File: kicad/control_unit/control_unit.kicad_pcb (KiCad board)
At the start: 2 copper layers, 23 parts

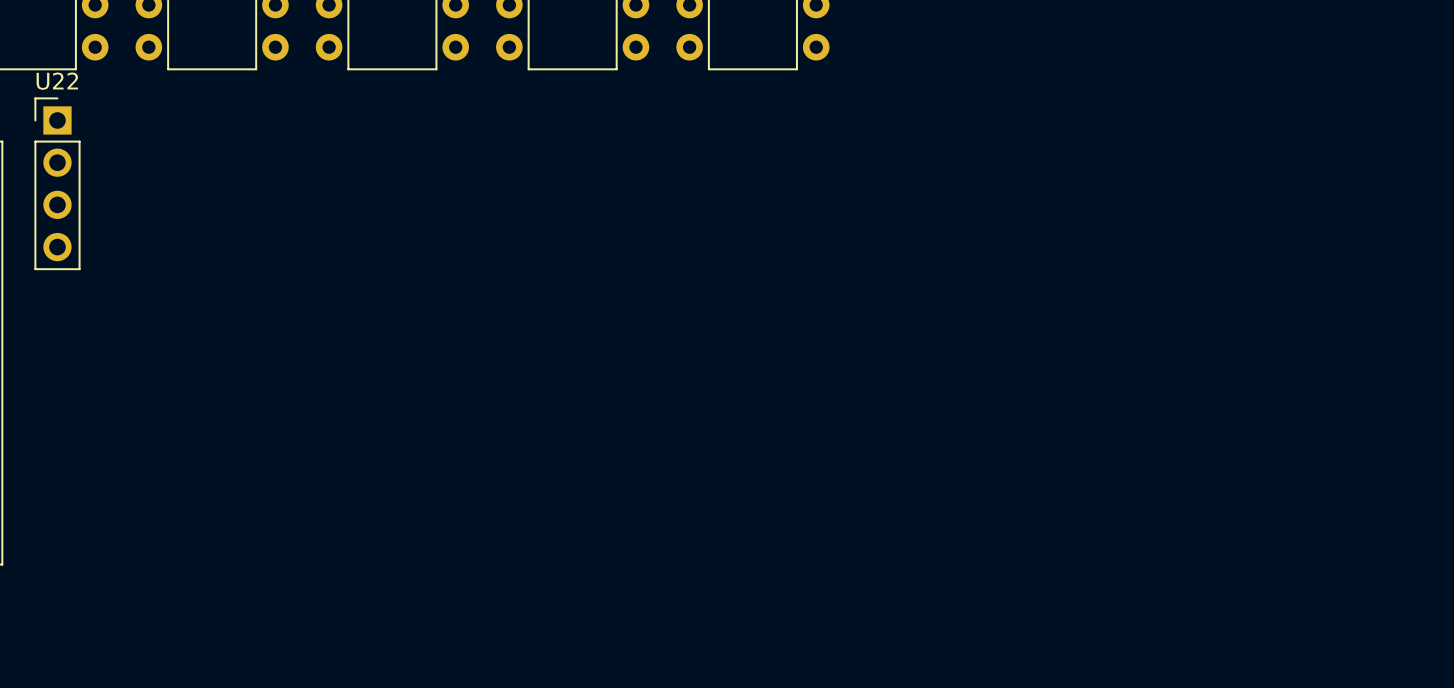
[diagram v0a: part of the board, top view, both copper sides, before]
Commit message: Added pullup resistors to control unit memory address
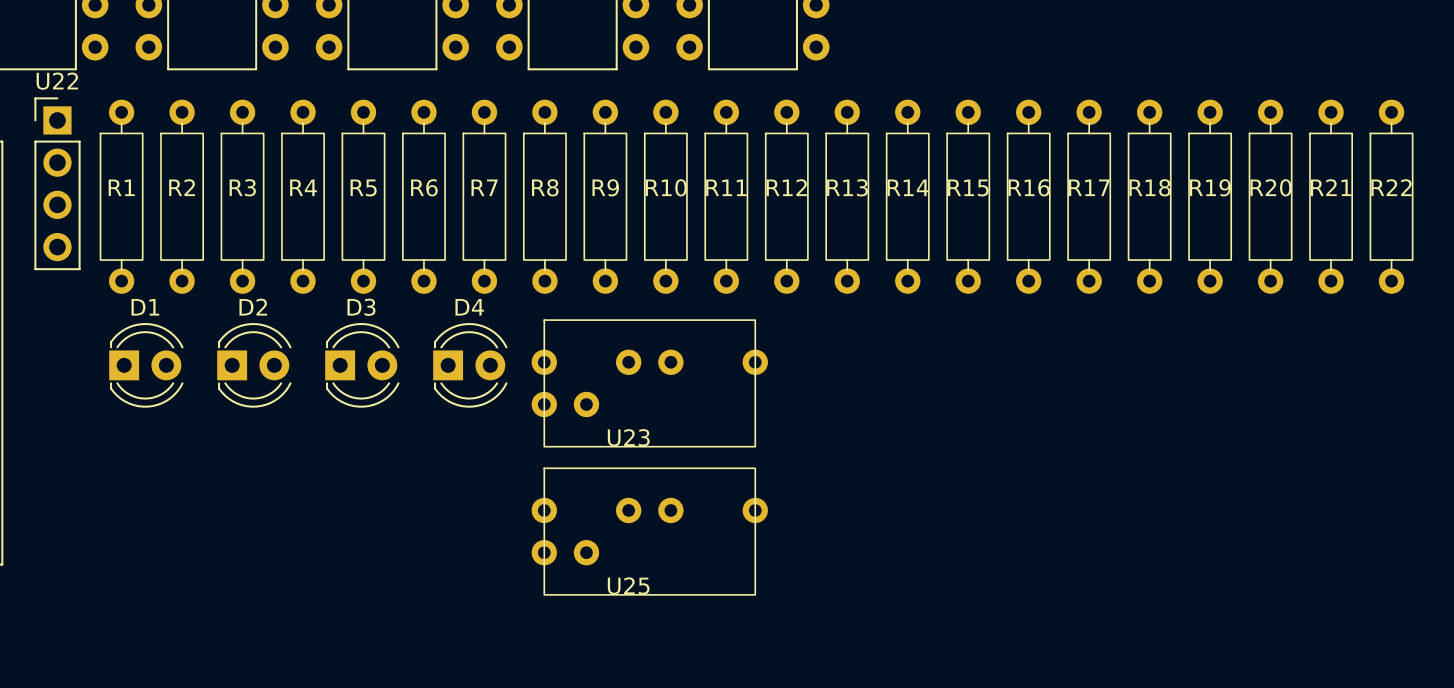
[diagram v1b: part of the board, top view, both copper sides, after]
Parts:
- added D1: LED, LED_THT:LED_D4.0mm, F.Cu at (138.3, 137.2)
- added D2: LED, LED_THT:LED_D4.0mm, F.Cu at (144.8, 137.2)
- added D3: LED, LED_THT:LED_D4.0mm, F.Cu at (151.3, 137.2)
- added D4: LED, LED_THT:LED_D4.0mm, F.Cu at (157.8, 137.2)
- added R1: 10k, custom_footprint_library:0.4_pitch_resistor, F.Cu at (138.2, 127.0)
- added R10: 10k, custom_footprint_library:0.4_pitch_resistor, F.Cu at (170.9, 127.0)
- added R11: 10k, custom_footprint_library:0.4_pitch_resistor, F.Cu at (174.6, 127.0)
- added R12: 10k, custom_footprint_library:0.4_pitch_resistor, F.Cu at (178.2, 127.0)
- added R13: 10k, custom_footprint_library:0.4_pitch_resistor, F.Cu at (181.9, 127.0)
- added R14: 10k, custom_footprint_library:0.4_pitch_resistor, F.Cu at (185.5, 127.0)
- added R15: 10k, custom_footprint_library:0.4_pitch_resistor, F.Cu at (189.2, 127.0)
- added R16: 10k, custom_footprint_library:0.4_pitch_resistor, F.Cu at (192.8, 127.0)
- added R17: 10k, custom_footprint_library:0.4_pitch_resistor, F.Cu at (196.4, 127.0)
- added R18: 10k, custom_footprint_library:0.4_pitch_resistor, F.Cu at (200.1, 127.0)
- added R19: 10k, custom_footprint_library:0.4_pitch_resistor, F.Cu at (203.7, 127.0)
- added R2: 10k, custom_footprint_library:0.4_pitch_resistor, F.Cu at (141.8, 127.0)
- added R20: 10k, custom_footprint_library:0.4_pitch_resistor, F.Cu at (207.3, 127.0)
- added R21: 10k, custom_footprint_library:0.4_pitch_resistor, F.Cu at (211.0, 127.0)
- added R22: 10k, custom_footprint_library:0.4_pitch_resistor, F.Cu at (214.6, 127.0)
- added R3: 10k, custom_footprint_library:0.4_pitch_resistor, F.Cu at (145.5, 127.0)
- added R4: 10k, custom_footprint_library:0.4_pitch_resistor, F.Cu at (149.1, 127.0)
- added R5: 10k, custom_footprint_library:0.4_pitch_resistor, F.Cu at (152.8, 127.0)
- added R6: 10k, custom_footprint_library:0.4_pitch_resistor, F.Cu at (156.4, 127.0)
- added R7: 10k, custom_footprint_library:0.4_pitch_resistor, F.Cu at (160.0, 127.0)
- added R8: 10k, custom_footprint_library:0.4_pitch_resistor, F.Cu at (163.7, 127.0)
- added R9: 10k, custom_footprint_library:0.4_pitch_resistor, F.Cu at (167.3, 127.0)
- added U23: ~, custom_footprint_library:jumper, F.Cu at (168.7, 142.0)
- added U25: ~, custom_footprint_library:jumper, F.Cu at (168.7, 151.0)
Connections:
- U1 pad 13: Net-(U1-GND) -> Net-(D1-K)
- U10 pad 10: Net-(U1-GND) -> Net-(D1-K)
- U10 pad 13: Net-(U1-GND) -> Net-(D1-K)
- U10 pad 15: Net-(U1-GND) -> Net-(D1-K)
- U10 pad 8: Net-(U1-GND) -> Net-(D1-K)
- U11 pad 2: Net-(U1-GND) -> Net-(D1-K)
- U12 pad 7: Net-(U1-GND) -> Net-(D1-K)
- U13 pad 11: Net-(U1-GND) -> Net-(D1-K)
- U13 pad 15: Net-(U1-GND) -> Net-(D1-K)
- U13 pad 2: Net-(U1-GND) -> Net-(D1-K)
- U13 pad 6: Net-(U1-GND) -> Net-(D1-K)
- U13 pad 8: Net-(U1-GND) -> Net-(D1-K)
- U14 pad 1: Net-(U1-GND) -> Net-(D1-K)
- U14 pad 2: Net-(U1-GND) -> Net-(D1-K)
- U14 pad 5: Net-(U1-GND) -> Net-(D1-K)
- U14 pad 6: Net-(U1-GND) -> Net-(D1-K)
- U14 pad 7: Net-(U1-GND) -> Net-(D1-K)
- U14 pad 8: Net-(U1-GND) -> Net-(D1-K)
- U14 pad 9: Net-(U1-GND) -> Net-(D1-K)
- U15 pad 8: Net-(U1-GND) -> Net-(D1-K)
- U16 pad 7: Net-(U1-GND) -> Net-(D1-K)
- U16 pad 8: Net-(U1-READ_READY) -> Net-(U16-4Q)
- U17 pad 2: Net-(U1-GND) -> Net-(D1-K)
- U17 pad 4: Net-(U1-GND) -> Net-(D1-K)
- U17 pad 6: Net-(U12-3B) -> Net-(U17-Done)
- U17 pad 7: Net-(U1-GND) -> Net-(U1-V+)
- U18 pad 11: Net-(U1-GND) -> Net-(D1-K)
- U18 pad 15: Net-(U1-GND) -> Net-(D1-K)
- U18 pad 2: Net-(U1-GND) -> Net-(D1-K)
- U18 pad 6: Net-(U1-GND) -> Net-(D1-K)
- U18 pad 8: Net-(U1-GND) -> Net-(D1-K)
- U19 pad 10: Net-(U1-GND) -> Net-(D1-K)
- U20 pad 1: unconnected-(U20-I0-Pad1) -> Net-(D1-K)
- U20 pad 3: unconnected-(U20-I1-Pad3) -> Net-(D1-K)
- U20 pad 5: unconnected-(U20-I2-Pad5) -> Net-(D1-K)
- U20 pad 7: Net-(U1-GND) -> Net-(D1-K)
- U21 pad 11: Net-(U1-GND) -> Net-(D1-K)
- U21 pad 15: Net-(U1-GND) -> Net-(D1-K)
- U21 pad 2: Net-(U1-GND) -> Net-(D1-K)
- U21 pad 7: Net-(U1-GND) -> Net-(D1-K)
- U21 pad 8: Net-(U1-GND) -> Net-(D1-K)
- U24 pad 10: Net-(U1-GND) -> Net-(D1-K)
- U3 pad 2: Net-(U1-GND) -> Net-(D1-K)
- U3 pad 3: Net-(U11-CALL_STACK-POP) -> Net-(U11-CALL_STACK-PUSH)
- U3 pad 4: Net-(U11-CALL_STACK-PUSH) -> Net-(U11-CALL_STACK-POP)
- U4 pad 10: Net-(U1-GND) -> Net-(D1-K)
- U4 pad 11: Net-(U1-GND) -> Net-(D1-K)
- U4 pad 4: Net-(U1-GND) -> Net-(D1-K)
- U4 pad 6: Net-(U1-GND) -> Net-(D1-K)
- U4 pad 7: Net-(U1-GND) -> Net-(D1-K)
- U4 pad 8: Net-(U1-GND) -> Net-(D1-K)
- U4 pad 9: Net-(U1-GND) -> Net-(D1-K)
- U5 pad 10: Net-(U1-GND) -> Net-(D1-K)
- U6 pad 1: Net-(U1-GND) -> Net-(D1-K)
- U6 pad 10: Net-(U1-GND) -> Net-(D1-K)
- U7 pad 10: Net-(U1-GND) -> Net-(D1-K)
- U8 pad 10: Net-(U1-GND) -> Net-(D1-K)
- U9 pad 1: Net-(U1-GND) -> Net-(D1-K)
- U9 pad 10: Net-(U1-GND) -> Net-(D1-K)

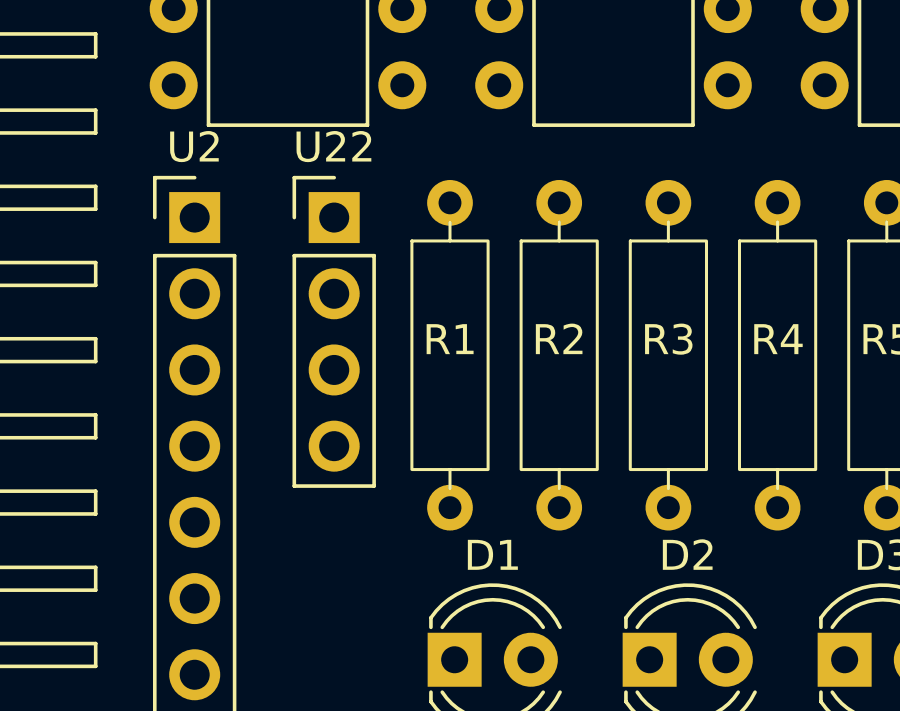
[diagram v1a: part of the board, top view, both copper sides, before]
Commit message: Working on GPRAM schematic
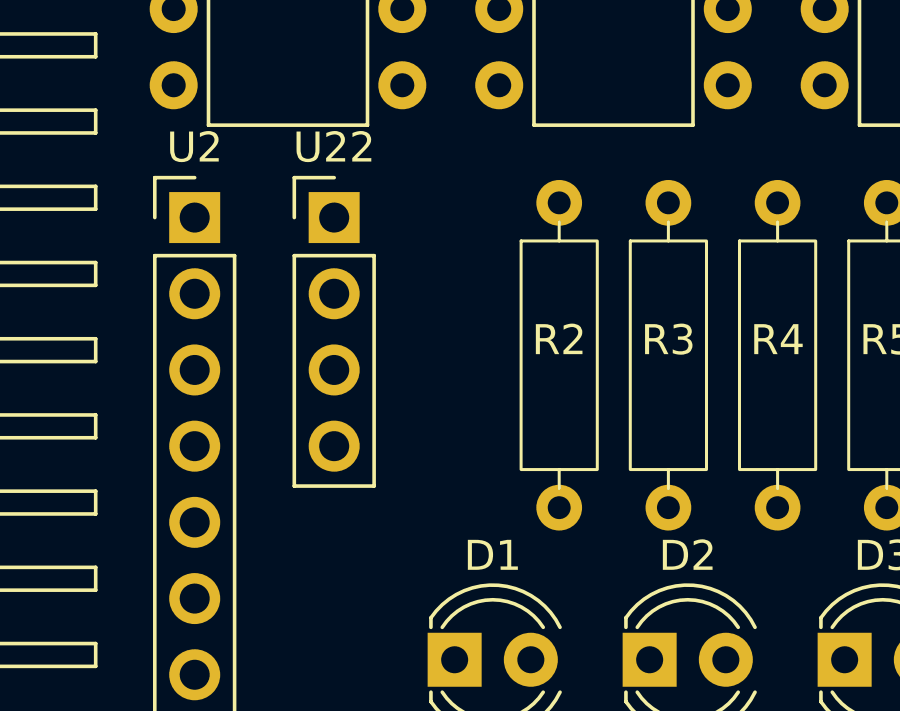
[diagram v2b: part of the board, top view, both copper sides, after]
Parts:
- removed R1: 10k, custom_footprint_library:0.4_pitch_resistor
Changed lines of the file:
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@@
 	(net 122 "Net-(U18-Σ3)")
 	(net 123 "Net-(U19-OE#)")
-	(net 124 "unconnected-(R1-Pad2)")
-	(net 125 "unconnected-(U20-O0-Pad2)")
-	(net 126 "unconnected-(U20-O1-Pad4)")
-	(net 127 "unconnected-(U20-O2-Pad6)")
-	(net 128 "unconnected-(R1-Pad1)")
-	(net 129 "Net-(U16-4Q)")
-	(net 130 "Net-(U21-Σ3)")
-	(net 131 "Net-(U21-Σ0)")
-	(net 132 "Net-(U21-Σ2)")
-	(net 133 "Net-(U21-Σ1)")
-	(net 134 "Net-(U17-Done)")
+	(net 124 "unconnected-(U20-O0-Pad2)")
+	(net 125 "unconnected-(U20-O1-Pad4)")
+	(net 126 "unconnected-(U20-O2-Pad6)")
+	(net 127 "Net-(U16-4Q)")
+	(net 128 "Net-(U21-Σ3)")
+	(net 129 "Net-(U21-Σ0)")
+	(net 130 "Net-(U21-Σ2)")
+	(net 131 "Net-(U21-Σ1)")
+	(net 132 "Net-(U17-Done)")
 	(footprint "LED_THT:LED_D4.0mm"
 		(layer "F.Cu")
@@
 			(layers "*.Cu" "*.Mask")
 			(remove_unused_layers no)
-			(net 129 "Net-(U16-4Q)")
+			(net 127 "Net-(U16-4Q)")
 			(pinfunction "IN")
 			(pintype "input")
@@
 			(layers "*.Cu" "*.Mask")
 			(remove_unused_layers no)
-			(net 129 "Net-(U16-4Q)")
+			(net 127 "Net-(U16-4Q)")
 			(pinfunction "IN")
 			(pintype "input")
@@
 			(layers "*.Cu" "*.Mask")
 			(remove_unused_layers no)
-			(net 134 "Net-(U17-Done)")
+			(net 132 "Net-(U17-Done)")
 			(pinfunction "Done")
 			(pintype "bidirectional")
@@
 			(layers "*.Cu" "*.Mask")
 			(remove_unused_layers no)
-			(net 129 "Net-(U16-4Q)")
+			(net 127 "Net-(U16-4Q)")
 			(pinfunction "4Q")
 			(pintype "output")
@@
 			(layers "*.Cu" "*.Mask")
 			(remove_unused_layers no)
-			(net 125 "unconnected-(U20-O0-Pad2)")
+			(net 124 "unconnected-(U20-O0-Pad2)")
 			(pinfunction "O0")
 			(pintype "output+no_connect")
@@
 			(layers "*.Cu" "*.Mask")
 			(remove_unused_layers no)
-			(net 126 "unconnected-(U20-O1-Pad4)")
+			(net 125 "unconnected-(U20-O1-Pad4)")
 			(pinfunction "O1")
 			(pintype "output+no_connect")
@@
 			(layers "*.Cu" "*.Mask")
 			(remove_unused_layers no)
-			(net 127 "unconnected-(U20-O2-Pad6)")
+			(net 126 "unconnected-(U20-O2-Pad6)")
 			(pinfunction "O2")
 			(pintype "output+no_connect")
@@
 			(layers "*.Cu" "*.Mask")
 			(remove_unused_layers no)
-			(net 131 "Net-(U21-Σ0)")
+			(net 129 "Net-(U21-Σ0)")
 			(pinfunction "D0")
 			(pintype "input")
@@
 			(layers "*.Cu" "*.Mask")
 			(remove_unused_layers no)
-			(net 133 "Net-(U21-Σ1)")
+			(net 131 "Net-(U21-Σ1)")
 			(pinfunction "D1")
 			(pintype "input")
@@
 			(layers "*.Cu" "*.Mask")
 			(remove_unused_layers no)
-			(net 132 "Net-(U21-Σ2)")
+			(net 130 "Net-(U21-Σ2)")
 			(pinfunction "D2")
 			(pintype "input")
@@
 			(layers "*.Cu" "*.Mask")
 			(remove_unused_layers no)
-			(net 130 "Net-(U21-Σ3)")
+			(net 128 "Net-(U21-Σ3)")
 			(pinfunction "D3")
 			(pintype "input")
@@
 			(layers "*.Cu" "*.Mask")
 			(remove_unused_layers no)
-			(net 134 "Net-(U17-Done)")
+			(net 132 "Net-(U17-Done)")
 			(pinfunction "IN")
 			(pintype "input")
@@
 			(layers "*.Cu" "*.Mask")
 			(remove_unused_layers no)
-			(net 134 "Net-(U17-Done)")
+			(net 132 "Net-(U17-Done)")
 			(pinfunction "IN")
 			(pintype "input")
@@
 			(layers "*.Cu" "*.Mask")
 			(remove_unused_layers no)
-			(net 133 "Net-(U21-Σ1)")
+			(net 131 "Net-(U21-Σ1)")
 			(pinfunction "Σ1")
 			(pintype "output")
@@
 			(layers "*.Cu" "*.Mask")
 			(remove_unused_layers no)
-			(net 131 "Net-(U21-Σ0)")
+			(net 129 "Net-(U21-Σ0)")
 			(pinfunction "Σ0")
 			(pintype "output")
@@
 			(layers "*.Cu" "*.Mask")
 			(remove_unused_layers no)
-			(net 130 "Net-(U21-Σ3)")
+			(net 128 "Net-(U21-Σ3)")
 			(pinfunction "Σ3")
 			(pintype "output")
@@
 			(layers "*.Cu" "*.Mask")
 			(remove_unused_layers no)
-			(net 132 "Net-(U21-Σ2)")
+			(net 130 "Net-(U21-Σ2)")
 			(pinfunction "Σ2")
 			(pintype "output")
@@
 		)
 	)
-	(footprint "custom_footprint_library:0.4_pitch_resistor"
-		(layer "F.Cu")
-		(at 138.19 127)
-		(property "Reference" "R1"
-			(at 0 -0.5 0)
-			(unlocked yes)
-			(layer "F.SilkS")
-			(effects
-				(font
-					(size 1 1)
-					(thickness 0.1)
-				)
-			)
-		)
-		(property "Value" "10k"
-			(at 0 1 0)
-			(unlocked yes)
-			(layer "F.Fab")
-			(effects
-				(font
-					(size 1 1)
-					(thickness 0.15)
-				)
-			)
-		)
-		(property "Footprint" "custom_footprint_library:0.4_pitch_resistor"
-			(at 0 0 0)
-			(unlocked yes)
-			(layer "F.Fab")
-			(hide yes)
-			(effects
-				(font
-					(size 1 1)
-					(thickness 0.15)
-				)
-			)
-		)
-		(property "Datasheet" ""
-			(at 0 0 0)
-			(unlocked yes)
-			(layer "F.Fab")
-			(hide yes)
-			(effects
-				(font
-					(size 1 1)
-					(thickness 0.15)
-				)
-			)
-		)
-		(property "Description" "Resistor"
-			(at 0 0 0)
-			(unlocked yes)
-			(layer "F.Fab")
-			(hide yes)
-			(effects
-				(font
-					(size 1 1)
-					(thickness 0.15)
-				)
-			)
-		)
-		(property ki_fp_filters "R_*")
-		(sheetname "Root")
-		(sheetfile "control_unit.kicad_sch")
-		(attr through_hole)
-		(fp_line
-			(start 0 -3.81)
-			(end 0 -4.445)
-			(stroke
-				(width 0.1)
-				(type default)
-			)
-			(layer "F.SilkS")
-		)
-		(fp_line
-			(start 0 4.445)
-			(end 0 3.81)
-			(stroke
-				(width 0.1)
-				(type default)
-			)
-			(layer "F.SilkS")
-		)
-		(fp_rect
-			(start -1.27 -3.81)
-			(end 1.27 3.81)
-			(stroke
-				(width 0.1)
-				(type default)
-			)
-			(fill none)
-			(layer "F.SilkS")
-		)
-		(fp_rect
-			(start -1.27 -6.35)
-			(end 1.27 6.35)
-			(stroke
-				(width 0.05)
-				(type default)
-			)
-			(fill none)
-			(layer "F.CrtYd")
-		)
-		(fp_text user "${REFERENCE}"
-			(at 0 2.5 0)
-			(unlocked yes)
-			(layer "F.Fab")
-			(effects
-				(font
-					(size 1 1)
-					(thickness 0.15)
-				)
-			)
-		)
-		(pad "1" thru_hole circle
-			(at 0 -5.08)
-			(size 1.524 1.524)
-			(drill 0.762)
-			(layers "*.Cu" "*.Mask")
-			(remove_unused_layers no)
-			(net 128 "unconnected-(R1-Pad1)")
-			(pintype "passive")
-		)
-		(pad "2" thru_hole circle
-			(at 0 5.08)
-			(size 1.524 1.524)
-			(drill 0.762)
-			(layers "*.Cu" "*.Mask")
-			(remove_unused_layers no)
-			(net 124 "unconnected-(R1-Pad2)")
-			(pintype "passive")
-		)
-	)
